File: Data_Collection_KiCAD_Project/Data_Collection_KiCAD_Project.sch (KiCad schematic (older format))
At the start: 42 parts

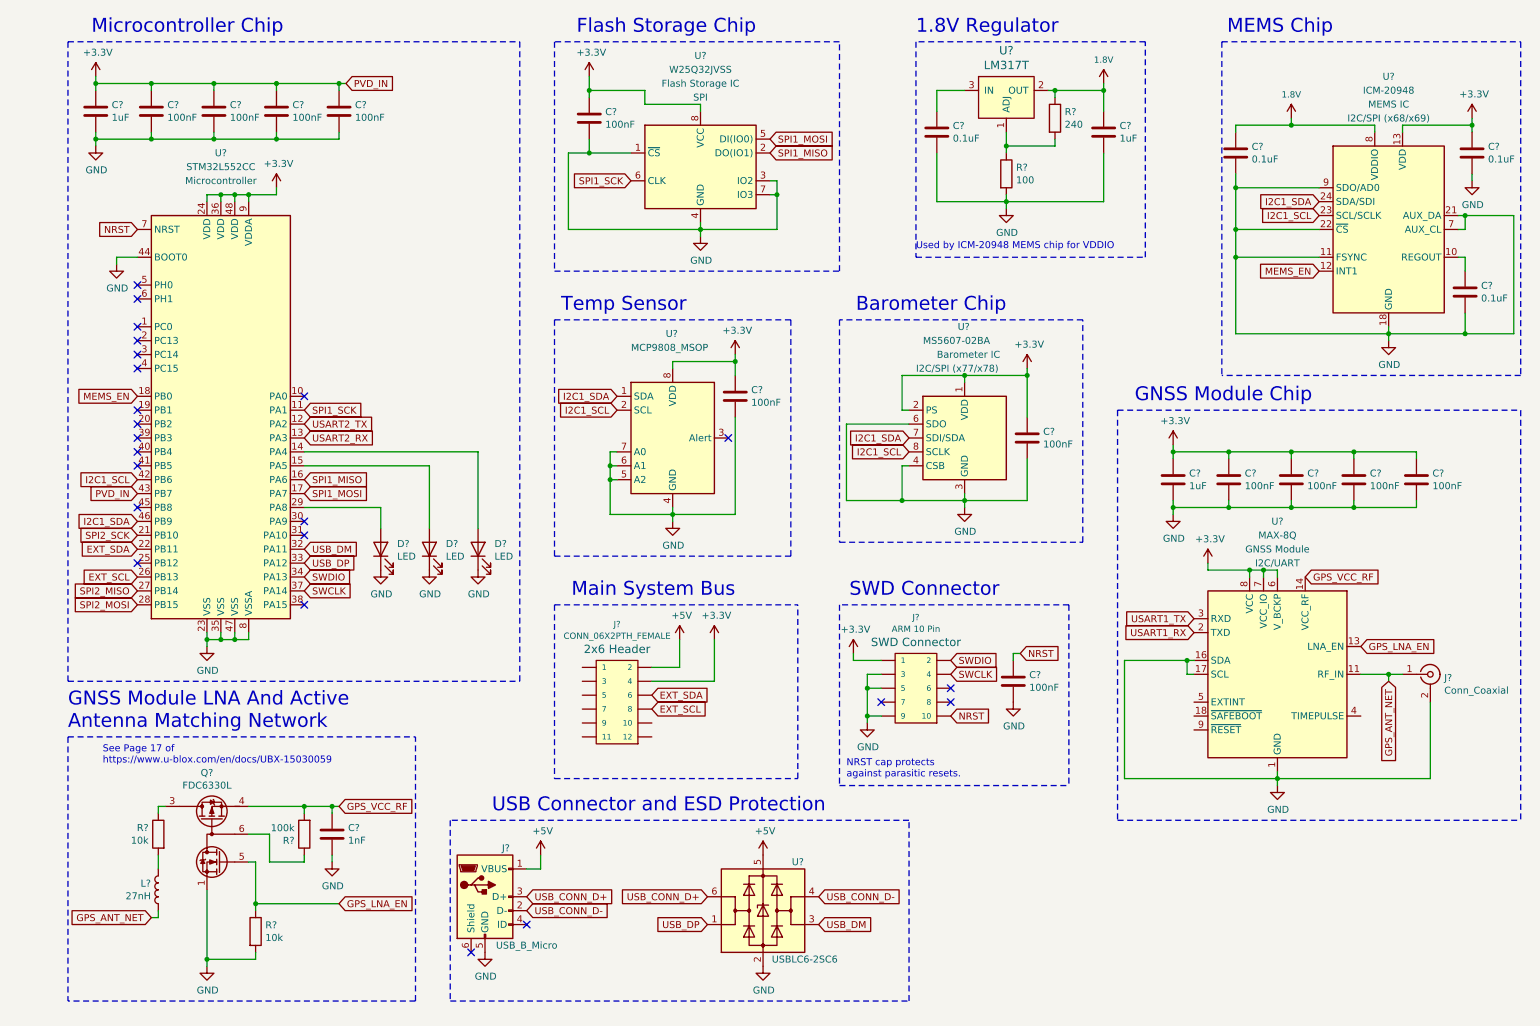
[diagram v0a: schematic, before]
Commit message: Schematic v1.0.1
Organized schematic into separate sheets. This helps modularize the project and eases switching between components as the design progresses.
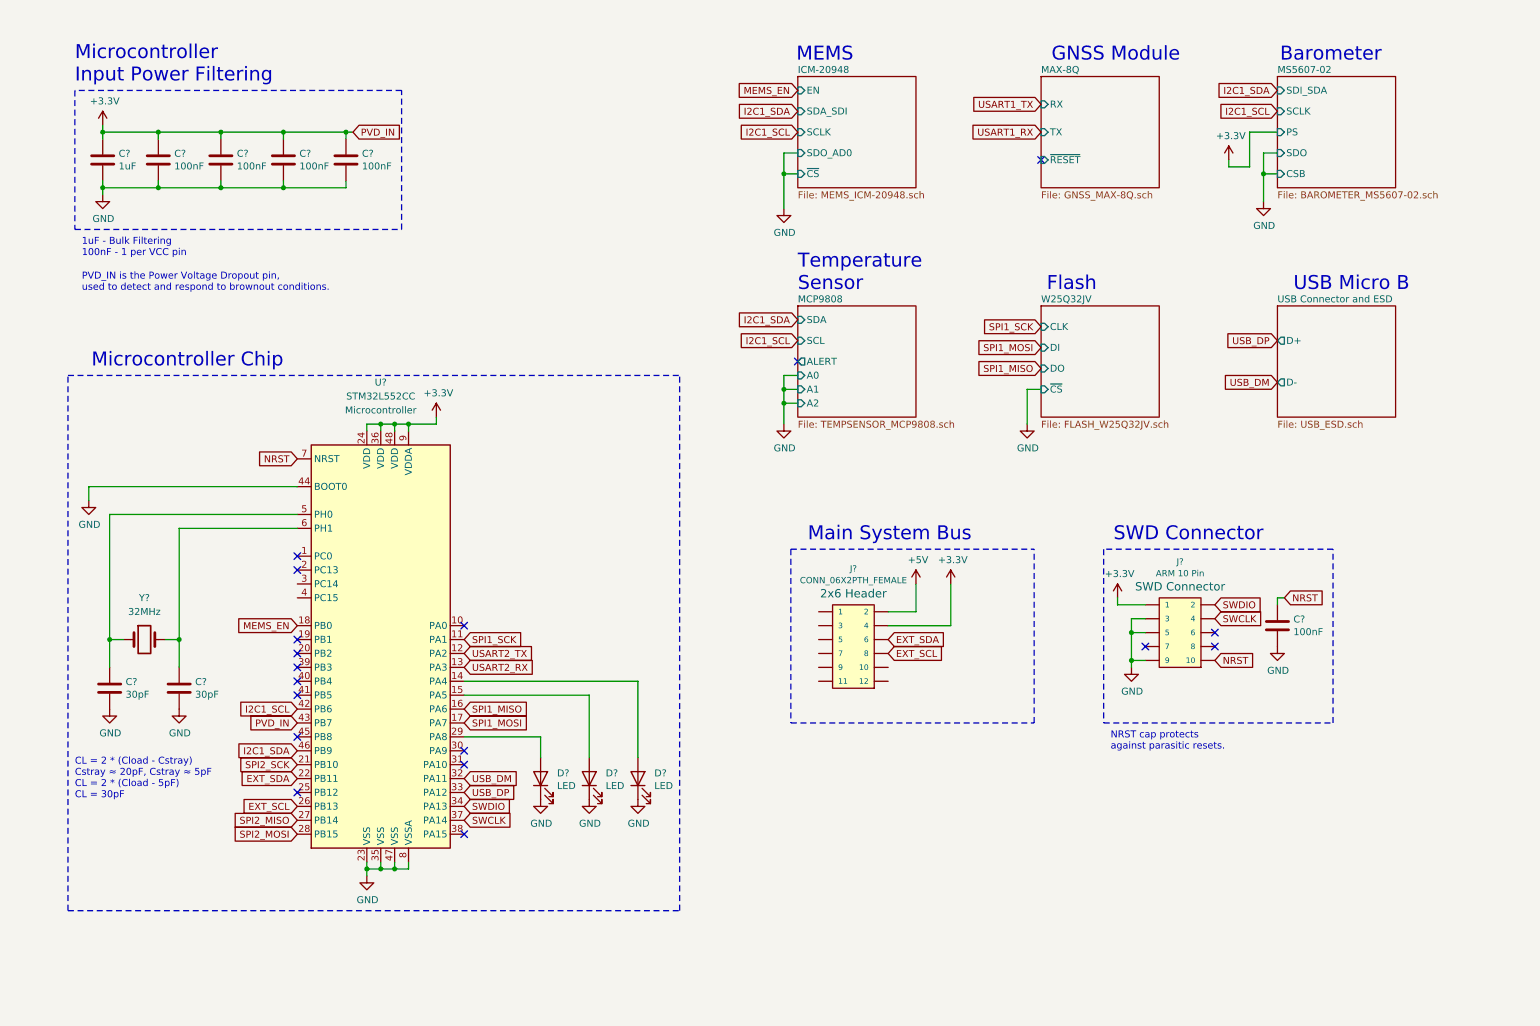
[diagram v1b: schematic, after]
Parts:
- removed C?: 1nF, symbol Device:C
- removed C? (x4): 0.1uF, symbol Device:C
- removed C? (x7): 100nF, symbol Device:C
- removed C? (x2): 1uF, symbol Device:C
- removed J?: Conn_Coaxial, symbol Connector:Conn_Coaxial
- removed J?: USB_B_Micro, symbol Connector:USB_B_Micro
- removed L?: 27nH, symbol Device:L
- removed Q?: FDC6330L, Package_TO_SOT_SMD:TSOT-23-6, symbol Transistor_FET:FDC6330L
- removed R?: 100k, symbol Device:R
- removed R? (x2): 10k, symbol Device:R
- removed R?: 240, symbol Device:R
- removed R?: 100, symbol Device:R
- removed U?: MS5607-02BA, Package_LGA:LGA-8_3x5mm_P1.25mm, symbol Sensor_Pressure:MS5607-02BA
- removed U?: MAX-8Q, RF_GPS:ublox_MAX, symbol RF_GPS:MAX-8Q
- removed U?: ICM-20948, Sensor_Motion:InvenSense_QFN-24_3x3mm_P0.4mm, symbol Sensor_Motion:ICM-20948
- removed U?: W25Q32JVSS, Package_SO:SOIC-8_5.23x5.23mm_P1.27mm, symbol Memory_Flash:W25Q32JVSS
- removed U?: USBLC6-2SC6, Package_TO_SOT_SMD:SOT-23-6, symbol Power_Protection:USBLC6-2SC6
- removed U?: LM317T, digikey-footprints:TO-220-3, symbol dk_PMIC-Voltage-Regulators-Linear:LM317T
- removed U?: MCP9808_MSOP, Package_SO:MSOP-8_3x3mm_P0.65mm, symbol Sensor_Temperature:MCP9808_MSOP
- added C? (x2): 30pF, symbol Device:C
- added Y?: 32MHz, symbol Device:Crystal
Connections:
- net GND: now also C?.2, C?.2
- net at U?.5 (PH0): now also C?.1, Y?.1
- net at U?.6 (PH1): now also C?.1, Y?.2
- no-connect marks 23 -> 18
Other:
- note added: "1uF - Bulk Filtering\n100nF - 1 per VCC pin"
- note added: "Barometer"
- note added: "CL = 2 * (Cload - Cstray)\nCstray ≈ 20pF, Cstray ≈ 5pF\nCL = 2 * (Cload - 5pF)\nCL = 30pF"
- note added: "Flash"
- note added: "GNSS Module"
- note added: "MEMS"
- note added: "Microcontroller\nInput Power Filtering"
- note added: "PVD_IN is the Power Voltage Dropout pin,\nused to detect and respond to brownout conditions."
- note added: "Temperature\nSensor"
- note added: "USB Micro B"
- note removed: "1.8V Regulator"
- note removed: "Barometer Chip"
- note removed: "Flash Storage Chip"
- note removed: "GNSS Module Chip"
- note removed: "GNSS Module LNA And Active\nAntenna Matching Network"
- note removed: "MEMS Chip"
- note removed: "See Page 17 of \nhttps://www.u-blox.com/en/docs/UBX-15030059"
- note removed: "Temp Sensor"
- note removed: "USB Connector and ESD Protection"
- note removed: "Used by ICM-20948 MEMS chip for VDDIO"
- moved on the sheet: C?, D?, J?, U?

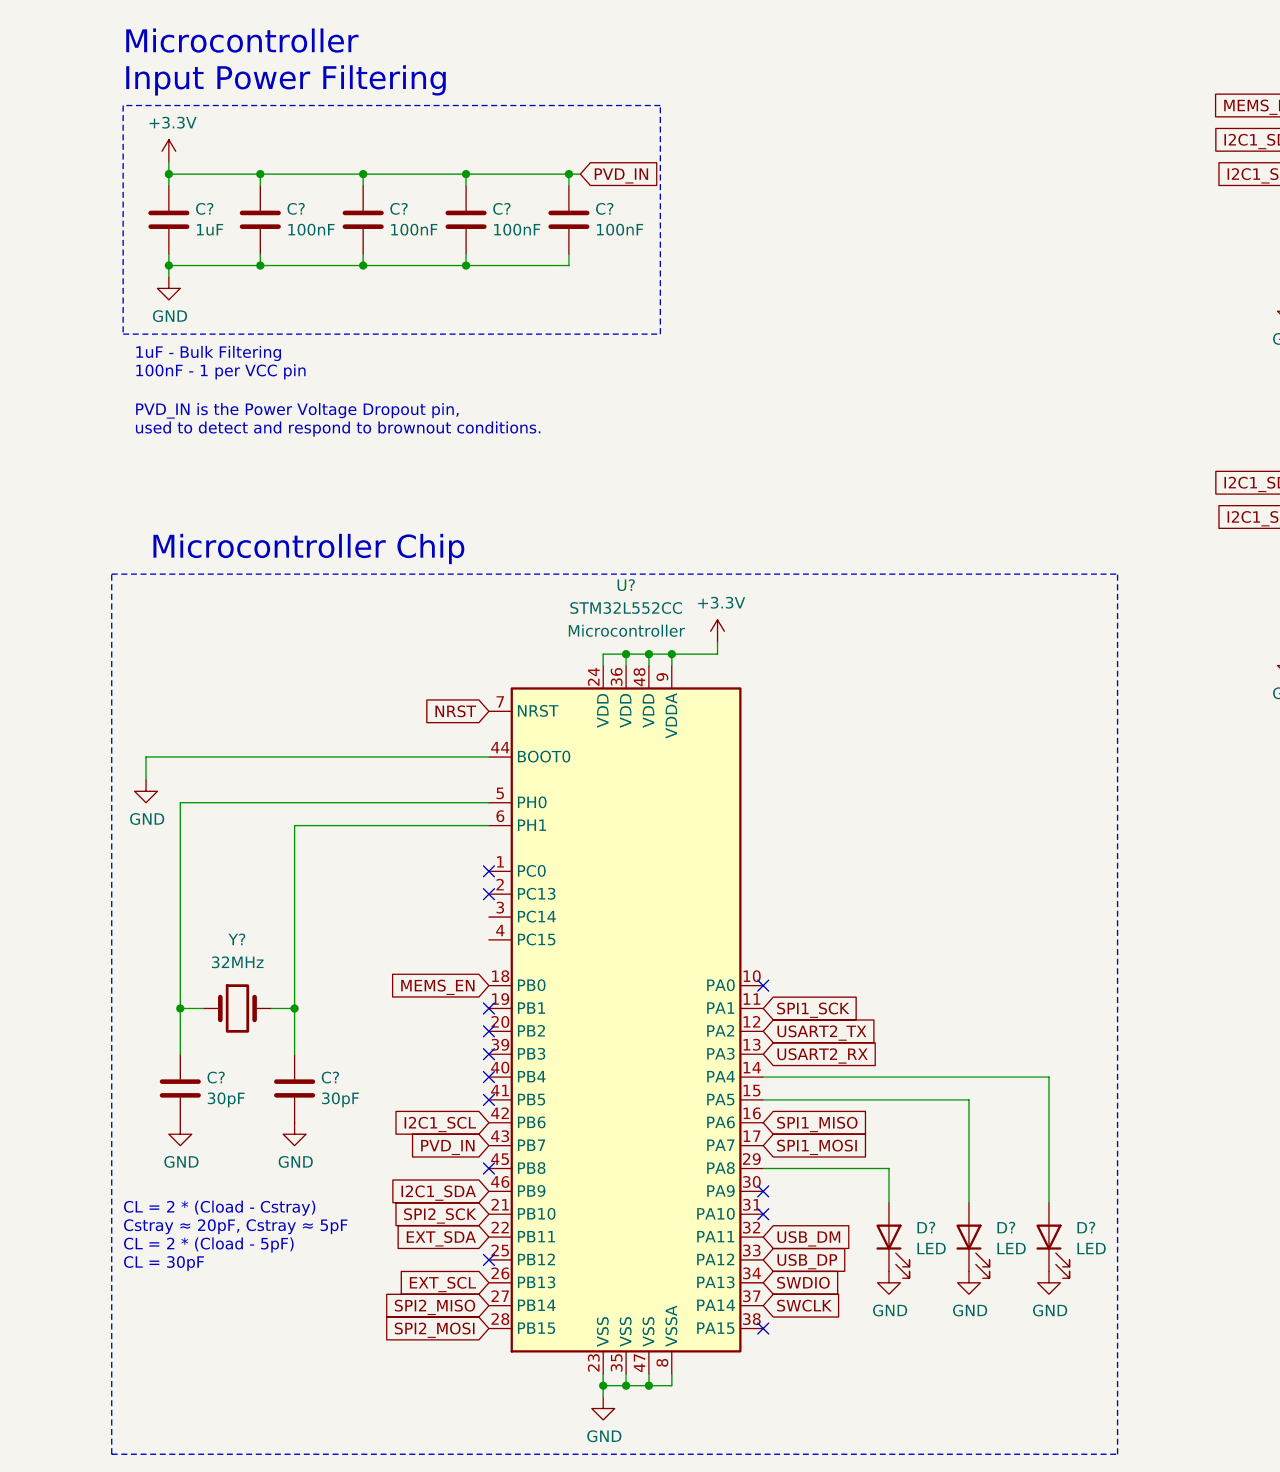
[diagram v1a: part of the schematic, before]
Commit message: Schematic v1.0.2
Moved MCU to separate sheet.
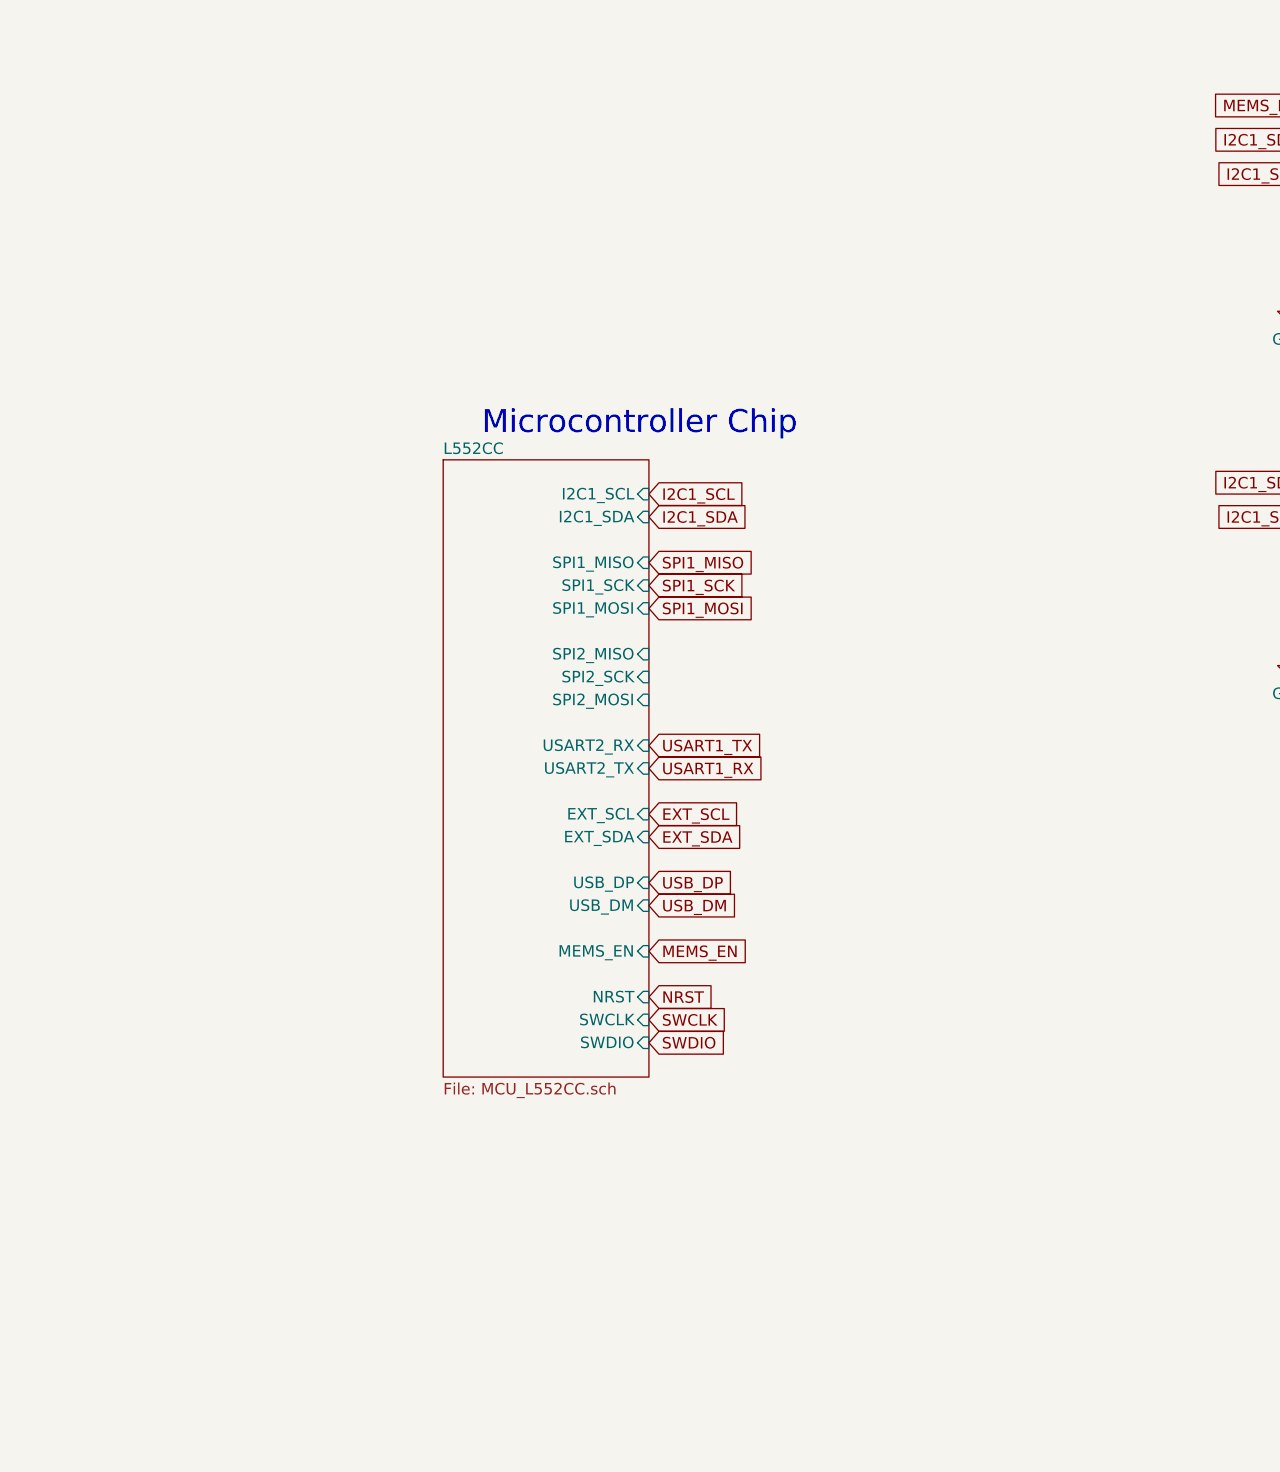
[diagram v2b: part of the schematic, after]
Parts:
- removed C?: 1uF, symbol Device:C
- removed C? (x4): 100nF, symbol Device:C
- removed C? (x2): 30pF, symbol Device:C
- removed D? (x3): LED, symbol Device:LED
- removed U?: STM32L552CC, Package_QFP:LQFP-48_7x7mm_P0.5mm, symbol MCU_ST_STM32L0:STM32L031C4Tx
- removed Y?: 32MHz, symbol Device:Crystal
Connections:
- no-connect marks 18 -> 5
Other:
- note removed: "1uF - Bulk Filtering\n100nF - 1 per VCC pin"
- note removed: "CL = 2 * (Cload - Cstray)\nCstray ≈ 20pF, Cstray ≈ 5pF\nCL = 2 * (Cload - 5pF)\nCL = 30pF"
- note removed: "Microcontroller\nInput Power Filtering"
- note removed: "PVD_IN is the Power Voltage Dropout pin,\nused to detect and respond to brownout conditions."
